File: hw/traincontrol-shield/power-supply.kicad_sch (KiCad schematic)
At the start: 0 parts

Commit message: Phase 3+4 complete: implement all 8 schematics, fix KiCad 9 lib embedding
All 7 sub-sheets and top-level sheet fully implemented and validated with
kicad-cli (exit 0 on all 8 files).

Key fixes to lib_sym_entry() in generator scripts:
- Sub-symbol names must NOT include library prefix (KiCad 9 parser requirement)
- Local KiCad 6 library symbols upgraded inline: remove (id N) from properties,
  strip stroke colors, fix bare 'hide', add exclude_from_sim + embedded_fonts
- Derived symbols (MOC3021M extends MOC3010M) flattened by copying base
  graphics into derived, removing (extends ...) for standalone embedding

Validated: kicad-cli sch export netlist exits 0 for all 8 .kicad_sch files.

Co-Authored-By: Claude Sonnet 4.6 <noreply@anthropic.com>
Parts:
- added C1: 220µF, Capacitor_THT:CP_Radial_D8.0mm_P3.50mm, symbol Device:C_Polarized
- added C2: 22µF, Capacitor_SMD:C_0603_1608Metric, symbol Device:C
- added C3, C9: 100nF, Capacitor_SMD:C_0603_1608Metric, symbol Device:C
- added D1: DB107, traincontrol-shield:DIO-BG-TH_DF, symbol traincontrol-shield:DB107
- added L1: 4.7µH, Inductor_SMD:L_0805_2012Metric, symbol Device:L
- added R12: 150kΩ, Resistor_SMD:R_0603_1608Metric, symbol Device:R
- added R13: 47kΩ, Resistor_SMD:R_0603_1608Metric, symbol Device:R
- added U1: MP2359DJ, traincontrol-shield:SOT-23-6_L2.9-W1.6-P0.95-LS2.8-BR, symbol traincontrol-shield:MP2359DJ-LF-Z
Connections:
- new net +15V: C1.2, C3.2, D1.2 (-), U1.5 (IN), U1.6 (SW)
- new net +3V3: C2.2, L1.1, R12.1
- new net AC_IN: D1.4
- new net AC_RTN: D1.3
- new net GND: C1.1, C2.1, C3.1, D1.1 (+), R13.2, U1.2 (GND)
- new net VBST: C9.2, U1.3 (FB)
- new net VFB: R12.2, R13.1, U1.1 (BST)
- new net VSW: C9.1, L1.2, U1.4 (EN)
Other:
- title: Traincontrol Shield — Power Supply -> Power Supply

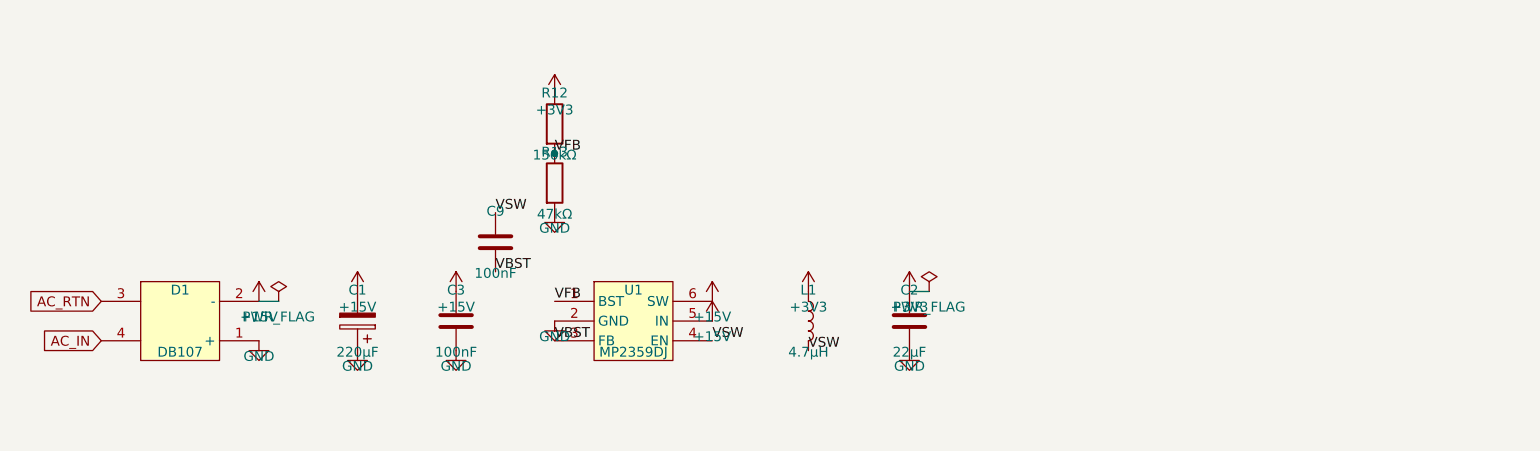
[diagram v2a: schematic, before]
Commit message: Add 2.54mm wire stubs to all power and global label connections
Power symbols (GND/+V) and global labels were placed directly on
component pins, making connections invisible in KiCad GUI. Add a
2.54mm stub wire between each component pin and power symbol/label
so connections are visually distinct. GND stubs go down (+y), +V
stubs go up (-y), label stubs go horizontally away from pin.
PWR_FLAG symbols are excluded (already have explicit wires).

All 8 schematics validate with kicad-cli exit 0.

Co-Authored-By: Claude Sonnet 4.6 <noreply@anthropic.com>
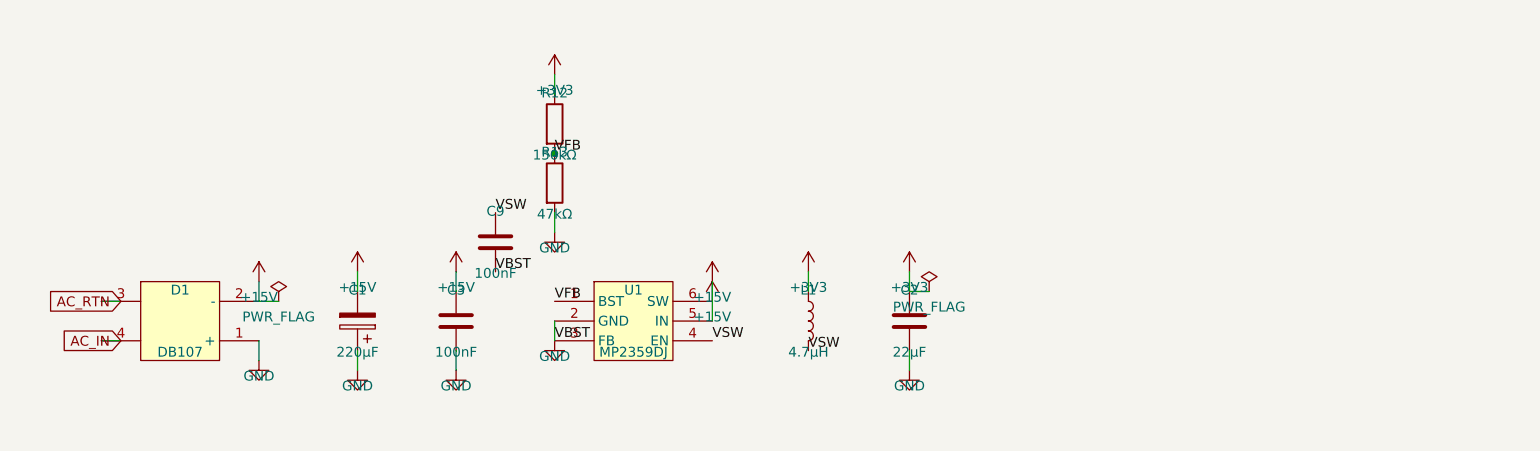
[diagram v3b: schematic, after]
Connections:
- net VBST is gone; now on net GND: C9.2, U1.3 (FB)

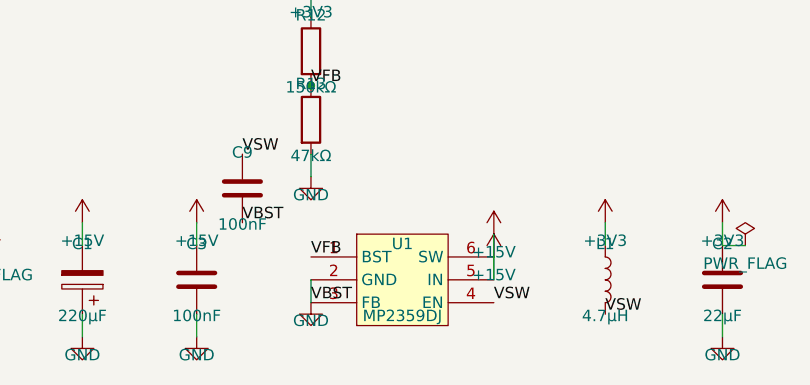
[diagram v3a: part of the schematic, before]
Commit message: Fix stub conflicts: prevent accidental cross-net connections
Power symbol stubs were landing on adjacent component pins,
creating unintended net connections (e.g. GND→VBST, GND→ZC_OUT,
+3V3→CTRL_A, +3V3→VSENSE, GND→GPIO20/GPIO12).

Fixes applied:
- power-supply: U1 GND (pin2) routed left 2.54mm (BST pin1 was
  directly below); U1 IN (pin5) +15V routed right 2.54mm (EN
  pin4 +15V was directly above at same x).
- zero-crossing: U2 GND (pin4) routed right 2.54mm (pin5/ZC_OUT
  was directly below at same x).
- mcu: all J1/J2 connector power pins (GND, +3V3) routed left
  2.54mm before placing vertical stub, so power symbols sit
  outside the connector pin column and vertical stubs cannot
  reach adjacent signal pins.

All 8 schematics validated with kicad-cli (exit 0).

Co-Authored-By: Claude Sonnet 4.6 <noreply@anthropic.com>
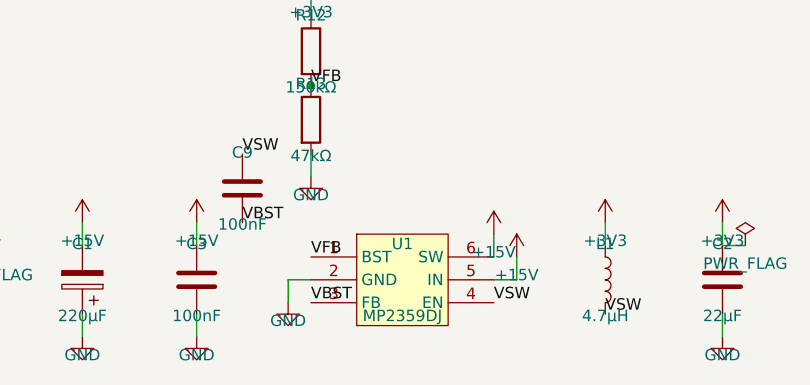
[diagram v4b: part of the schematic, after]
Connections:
- net GND: no longer C9.2, U1.3 (FB)
- new net VBST: C9.2, U1.3 (FB)
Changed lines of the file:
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@@
 	)
 	(wire
-		(pts (xy 99.06 68.58) (xy 99.06 71.12))
+		(pts (xy 99.06 68.58) (xy 96.52 68.58))
+		(stroke (width 0) (type solid))
+	)
+	(wire
+		(pts (xy 96.52 68.58) (xy 96.52 71.12))
 		(stroke (width 0) (type solid))
 	)
 	(symbol
 		(lib_id "power:GND")
-		(at 99.06 71.12 0)
+		(at 96.52 71.12 0)
 		(unit 1)
 		(exclude_from_sim no)
@@
 		(dnp no)
 		(property "Reference" "#PWR007"
-			(at 99.06 69.12 0)
+			(at 96.52 69.12 0)
 			(effects (font (size 1.27 1.27)) (hide yes))
 		)
 		(property "Value" "GND"
-			(at 99.06 73.12 0)
+			(at 96.52 73.12 0)
 			(effects (font (size 1.27 1.27)))
 		)
 		(property "Footprint" ""
-			(at 99.06 71.12 0)
+			(at 96.52 71.12 0)
 			(effects (font (size 1.27 1.27)) (hide yes))
 		)
 		(property "Datasheet" ""
-			(at 99.06 71.12 0)
+			(at 96.52 71.12 0)
 			(effects (font (size 1.27 1.27)) (hide yes))
 		)
@@
 	)
 	(wire
-		(pts (xy 119.38 68.58) (xy 119.38 66.03999999999999))
+		(pts (xy 119.38 68.58) (xy 121.92 68.58))
+		(stroke (width 0) (type solid))
+	)
+	(wire
+		(pts (xy 121.92 68.58) (xy 121.92 66.03999999999999))
 		(stroke (width 0) (type solid))
 	)
 	(symbol
 		(lib_id "power:+15V")
-		(at 119.38 66.03999999999999 0)
+		(at 121.92 66.03999999999999 0)
 		(unit 1)
 		(exclude_from_sim no)
@@
 		(dnp no)
 		(property "Reference" "#PWR009"
-			(at 119.38 64.03999999999999 0)
+			(at 121.92 64.03999999999999 0)
 			(effects (font (size 1.27 1.27)) (hide yes))
 		)
 		(property "Value" "+15V"
-			(at 119.38 68.03999999999999 0)
+			(at 121.92 68.03999999999999 0)
 			(effects (font (size 1.27 1.27)))
 		)
 		(property "Footprint" ""
-			(at 119.38 66.03999999999999 0)
+			(at 121.92 66.03999999999999 0)
 			(effects (font (size 1.27 1.27)) (hide yes))
 		)
 		(property "Datasheet" ""
-			(at 119.38 66.03999999999999 0)
+			(at 121.92 66.03999999999999 0)
 			(effects (font (size 1.27 1.27)) (hide yes))
 		)

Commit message: Add hierarchical ports to all sub-sheets and top-level connections
Replace inter-sheet global_label elements with hierarchical_label in all
sub-sheets, so each sheet exports visible ports on its sheet box symbol
in the top-level. Add matching (pin ...) entries to every sheet block in
the top-level. Connect all sheet pins with bidirectional global_labels in
the inter-column gap (x=105..120) so named nets auto-join.

Port counts per sub-sheet:
  power-supply:       2  (AC_IN, AC_RTN)
  zero-crossing:      3  (AC_IN, AC_RTN, ZC_OUT)
  xor-interlock:      6  (CTRL_A×2, CTRL_B×2, PHASE_A, PHASE_B)
  opto-triac-drive:   6  (PHASE_A, PHASE_B, AC_RTN×2, TRIAC_A_GATE, TRIAC_B_GATE)
  triacs-snubbers:   12  (AC_RTN×2, WINDING_A×3, WINDING_B×3, TRIAC_A_GATE, TRIAC_B_GATE)
  rail-voltage-sense: 1  (VSENSE)
  mcu:                4  (CTRL_A, CTRL_B, ZC_OUT, VSENSE)

All 8 schematics validate: kicad-cli exit 0.
Fix: correct KiCad 9 keyword is `hierarchical_label`, not `hier_label`.

Co-Authored-By: Claude Sonnet 4.6 <noreply@anthropic.com>
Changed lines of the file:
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@@
 		(stroke (width 0) (type solid))
 	)
-	(global_label "AC_IN"
+	(hierarchical_label "AC_IN"
 		(shape input)
 		(at 43.18 71.12 180)
@@
 		(stroke (width 0) (type solid))
 	)
-	(global_label "AC_RTN"
+	(hierarchical_label "AC_RTN"
 		(shape input)
 		(at 43.18 66.04 180)

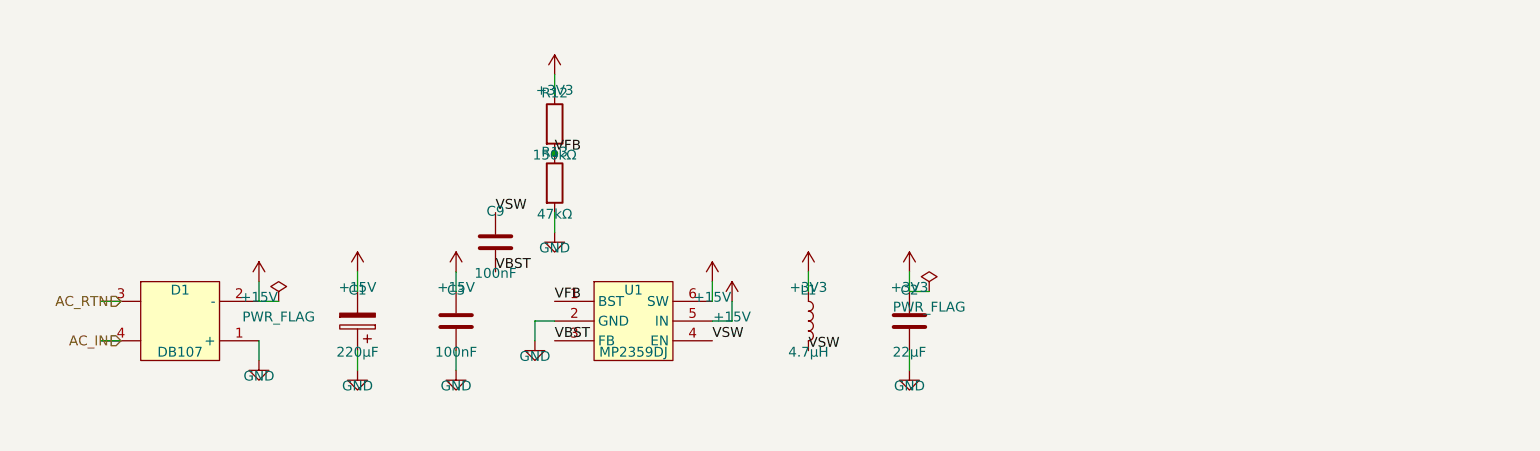
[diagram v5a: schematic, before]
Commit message: Disperse component layout and triple wire stub length across all sheets
- STUB: 2.54 → 7.62 mm (3×) in all three generator scripts
- Inter-component spacing doubled in power-supply, MCU, and logic sheets
- Top-level inter-column gap widened (LX 120 → 130 mm) to avoid label collision
- Sheet frame heights made variable per pin count (20–35 mm)
- Right-column sheet x-origin and connector J4/J5/J6 x-positions updated accordingly
- All 8 sheets regenerated and validated with kicad-cli

Co-Authored-By: Claude Sonnet 4.6 <noreply@anthropic.com>
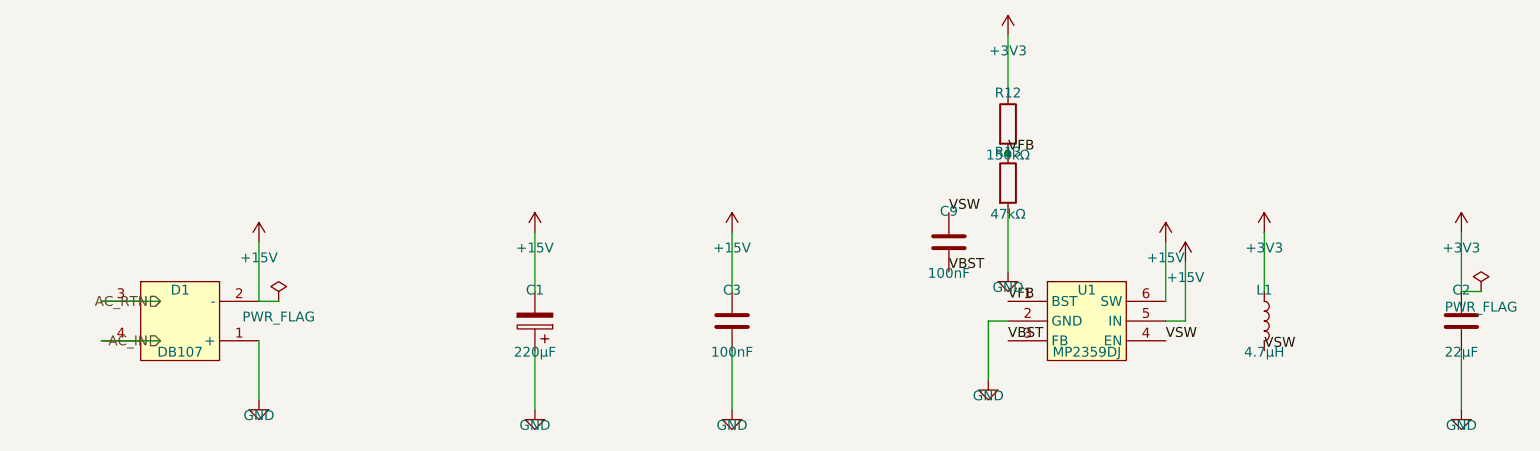
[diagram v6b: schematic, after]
